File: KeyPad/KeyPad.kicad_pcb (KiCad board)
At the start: 2 copper layers, 0 parts

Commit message: Pcb enrrutada y esquinas redondeadas
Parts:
- added P1: CONN_01X03, Connectors_JST:JST_PH_S3B-PH-K_03x2.00mm_Angled, F.Cu at (152.4, 119.4)
- added R1: 2K, Resistors_SMD:R_0805, F.Cu at (139.7, 102.2)
- added R2: 330R, Resistors_SMD:R_0805, F.Cu at (137.2, 102.2)
- added R3: 620R, Resistors_SMD:R_0805, F.Cu at (171.4, 102.2)
- added R4: 1K, Resistors_SMD:R_0805, F.Cu at (168.9, 102.2)
- added SW1: SW_Push_Dual, Buttons_Switches_THT:SW_PUSH-12mm, F.Cu at (143.3, 90.9)
- added SW2: SW_Push_Dual, Buttons_Switches_THT:SW_PUSH-12mm, F.Cu at (143.3, 112.8)
- added SW3: SW_Push_Dual, Buttons_Switches_THT:SW_PUSH-12mm, F.Cu at (165.1, 90.9)
- added SW4: SW_Push_Dual, Buttons_Switches_THT:SW_PUSH-12mm, F.Cu at (165.1, 112.8)
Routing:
- net Net-(R2-Pad2): track 0.00 -> 55.9 mm, vias 0 -> 1
- net Net-(P1-Pad2): track 0.00 -> 51.7 mm
- net Net-(R3-Pad2): track 0.00 -> 33.4 mm
- net VCC: track 0.00 -> 28.2 mm
- net Net-(R4-Pad2): track 0.00 -> 16.5 mm
- added copper zone on B.Cu, net GND
- added copper zone on F.Cu, net GND
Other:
- board outline added: 41.9 x 41.9 mm

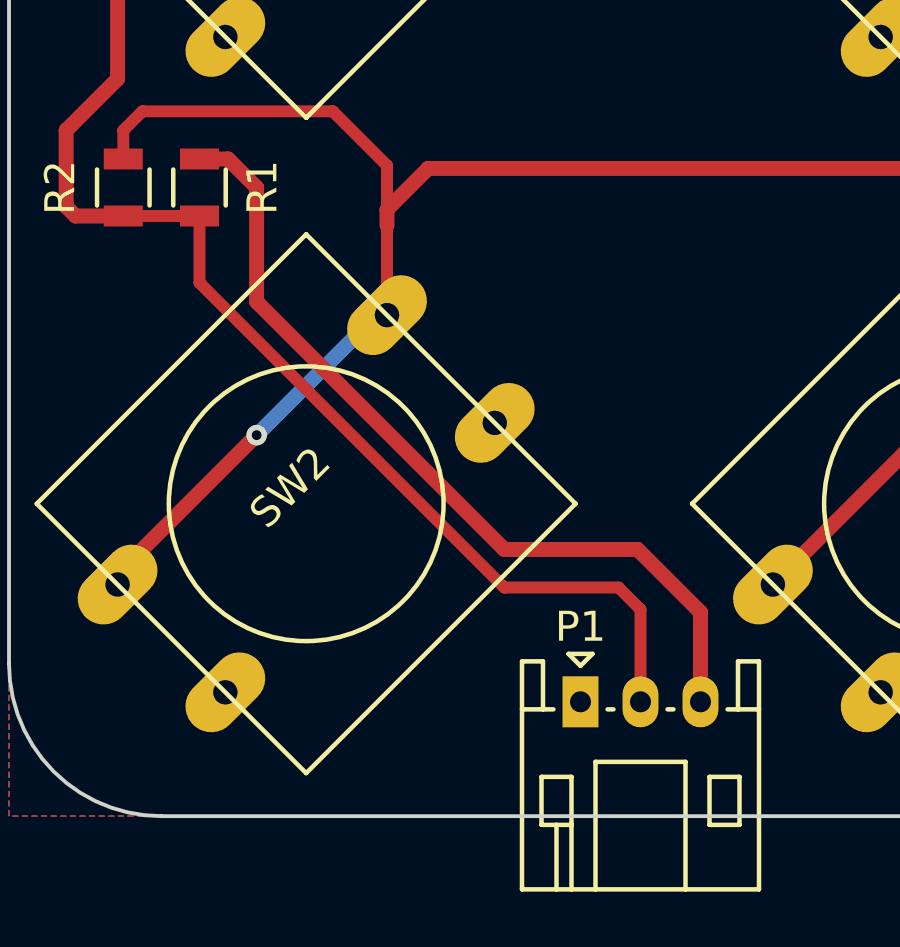
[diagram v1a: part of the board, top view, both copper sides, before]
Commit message: Error del conector reparado
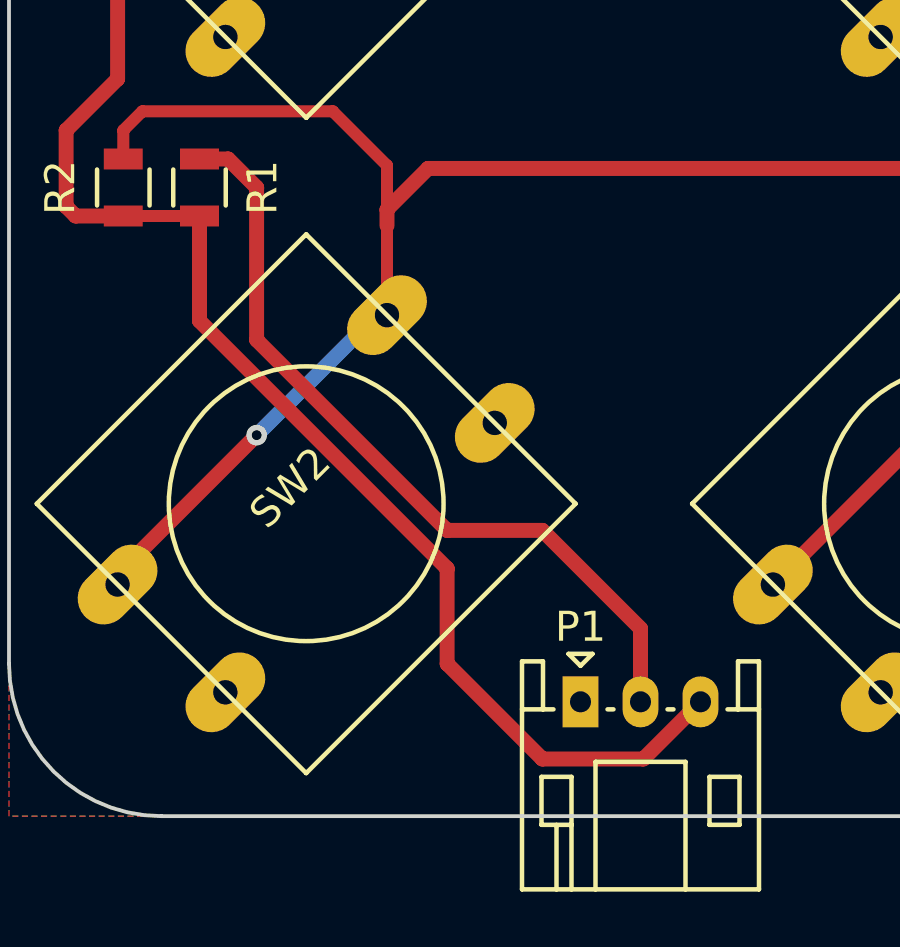
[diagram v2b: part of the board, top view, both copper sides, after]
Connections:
- P1 pad 2: Net-(P1-Pad2) -> VCC
- P1 pad 3: VCC -> Net-(P1-Pad3)
- R1 pad 2: Net-(P1-Pad2) -> Net-(P1-Pad3)
- R2 pad 1: Net-(P1-Pad2) -> Net-(P1-Pad3)
- SW1 pad 1: Net-(P1-Pad2) -> Net-(SW1-Pad1)
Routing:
- net Net-(P1-Pad2): track 51.7 -> 0.00 mm
- net Net-(P1-Pad3): track 0.00 -> 36.0 mm
- net Net-(SW1-Pad1): track 0.00 -> 20.1 mm
- net VCC: track 28.2 -> 26.6 mm

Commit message: Version final, taladros añadidos, serigrafia lista
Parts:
- added G***: LOGO, logos_frizzy:logo_glance, F.Cu at (154.3, 102.2)
- added G***: LOGO, logos_frizzy:logo_KeyPad, B.Cu at (154.3, 101.6)
- added G***: LOGO, logos_frizzy:web, B.Cu at (154.3, 83.8)
- added REF**: MountingHole_3.2mm_M3, Mounting_Holes:MountingHole_3.2mm_M3, F.Cu at (136.5, 120.0)
- added REF**: MountingHole_3.2mm_M3, Mounting_Holes:MountingHole_3.2mm_M3, F.Cu at (136.5, 84.5)
- added REF**: MountingHole_3.2mm_M3, Mounting_Holes:MountingHole_3.2mm_M3, F.Cu at (172.1, 84.5)
- added REF**: MountingHole_3.2mm_M3, Mounting_Holes:MountingHole_3.2mm_M3, F.Cu at (172.1, 120.0)
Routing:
- net Net-(R2-Pad2): track 55.9 -> 66.1 mm, vias 1 -> 2
- net Net-(SW1-Pad1): track 20.1 -> 17.7 mm
- net Net-(P1-Pad3): track 36.0 -> 38.4 mm
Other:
- board text added: "GND"
- board text added: "SIG"
- board text added: "VCC"
